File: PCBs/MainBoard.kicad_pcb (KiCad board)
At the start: 2 copper layers, 40.4 x 70 mm, 75 parts, among them J1 USB_C_Receptacle, J2 Conn_01x12_FPC_0.5mm, J3 Conn_01x08, J4 Qwiic_RA, SW1 PTH_RA_h7.5mm, SW2 SMD_4.6x2.8mm_h2.5mm, SW3 SMD_4.6x2.8mm_h2.5mm, U1 TVS_ESD_USB, U2 ESP32-S3-MINI, U3 AP3012, U4 MQ-4 Gas Sensor, U5 PASCO2V01BUMA1, U6 AP2112K-3.3, U7 MQ-7 Gas Sensor, U8 SEN55

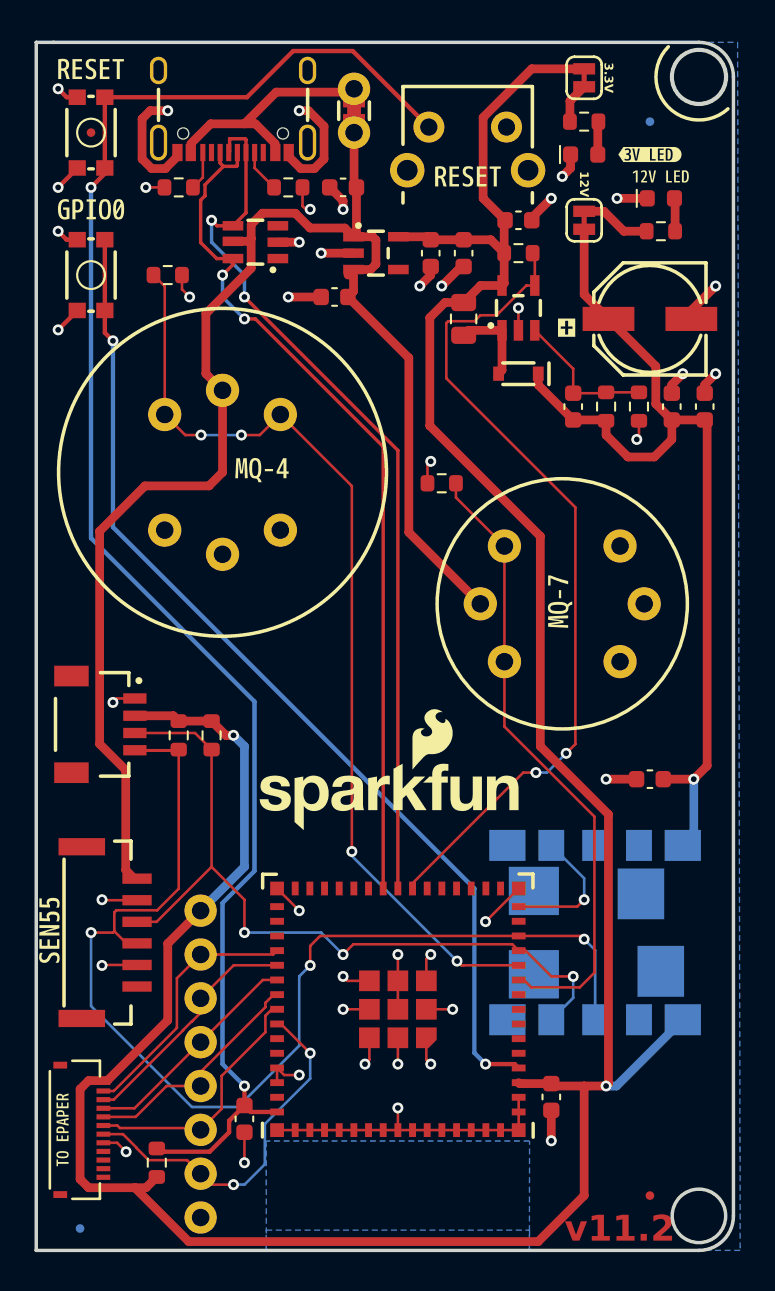
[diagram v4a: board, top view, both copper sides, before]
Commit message: Current PCB updates
Updated Main Board MQ sensors and external reset button position as well as SEN 55 connector pinout.
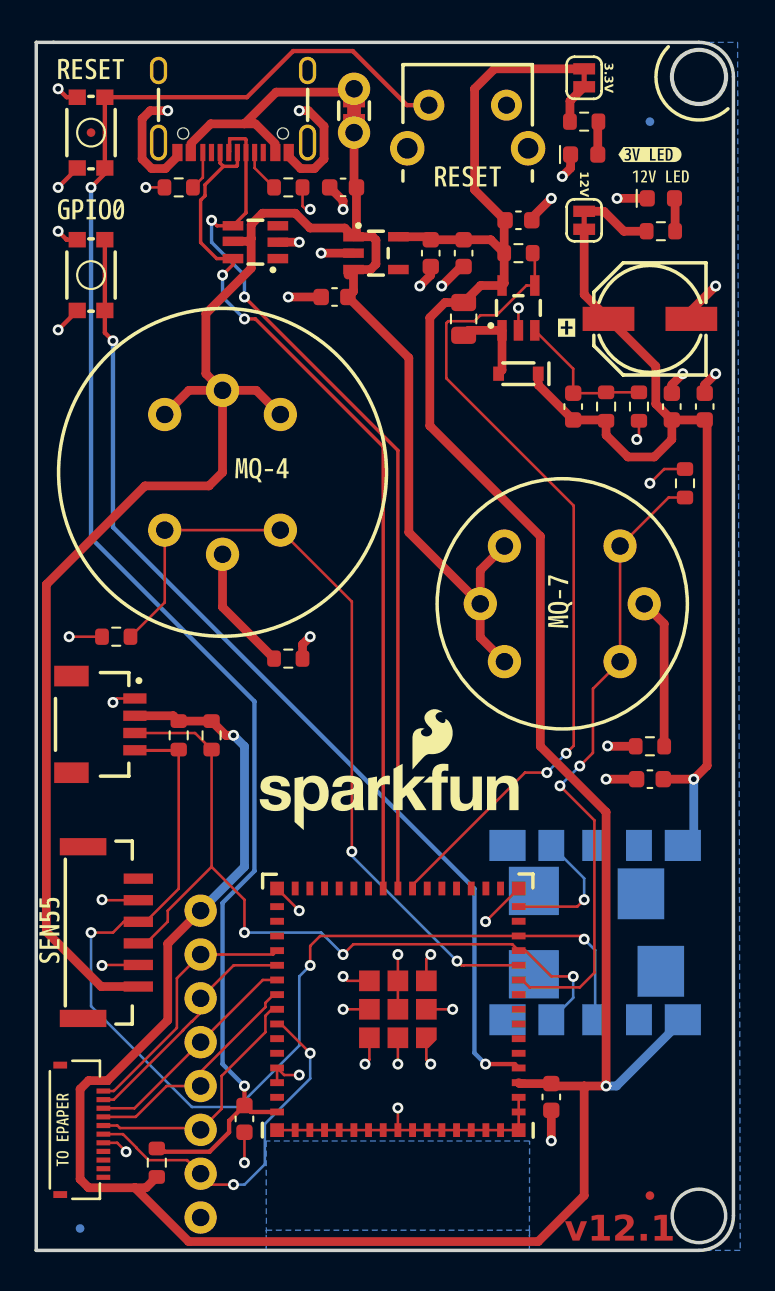
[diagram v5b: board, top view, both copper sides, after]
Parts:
- removed kibuzzard-65B1E438: G***, kibuzzard-65B1E438
- added R13: 100, SparkFun-Resistor:R_0603_1608Metric, F.Cu at (143.4, 89.6)
- added R14: 100, SparkFun-Resistor:R_0603_1608Metric, F.Cu at (164.4, 94.7)
- added kibuzzard-65E78438: G***, kibuzzard-65E78438, B.Cu at (148.9, 82.5)
- moved R7 21.2 mm to (133.4, 88.3), turned to 180 degrees
- moved R11 14.1 mm to (166.4, 79.5), turned to 90 degrees
- moved SW1 1.27 mm to (153.8, 57.5)
- moved U8 0.07 mm to (131.4, 105.5)
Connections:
- C7 pad +: (no net) -> +12V
- C7 pad -: (no net) -> GND
- U4 pad 1: ESP11/MQ4 -> +5V
- U4 pad 3: ESP11/MQ4 -> +5V
- U4 pad 4: GND -> ESP11/MQ4
- U4 pad 5: GND -> Net-(U4-H-)
- U4 pad 6: GND -> ESP11/MQ4
- U7 pad 1: ESP10/MQ7 -> +5V
- U7 pad 3: ESP10/MQ7 -> +5V
- U7 pad 4: GND -> ESP10/MQ7
- U7 pad 5: GND -> Net-(U7-H-)
- U7 pad 6: GND -> ESP10/MQ7
- U8 pad 1: +5V -> unconnected-(U8-NC-Pad1)
- U8 pad 3: SDA -> SCL
- U8 pad 4: SCL -> SDA
- U8 pad 6: unconnected-(U8-NC-Pad6) -> +5V
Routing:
- net +5V: track 86.9 -> 112.6 mm
- net ESP11/MQ4: track 55.7 -> 46.6 mm, vias 4 -> 2
- net Net-(U7-H-): track 0.00 -> 8.73 mm
- net Net-(U4-H-): track 0.00 -> 7.28 mm
- net GND: track 97.6 -> 102.1 mm, vias 43 -> 45
- net SCL: track 68.9 -> 66.8 mm
- net +3.3V: track 165.8 -> 167.3 mm
- net SDA: track 45.8 -> 46.3 mm
- net RESET: track 94.4 -> 93.9 mm
- net ESP10/MQ7: track 36.6 -> 36.8 mm, vias 0 -> 2
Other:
- board text added: "v12.1"
- board text removed: "v11.2"

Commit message: Screen and Main Board Updates
Updated Main board to Screen PCB connection, added accelerometer to Epaper display PCB. Removed GPIO 0 PB and replaced external Reset button with GPIO0 button.
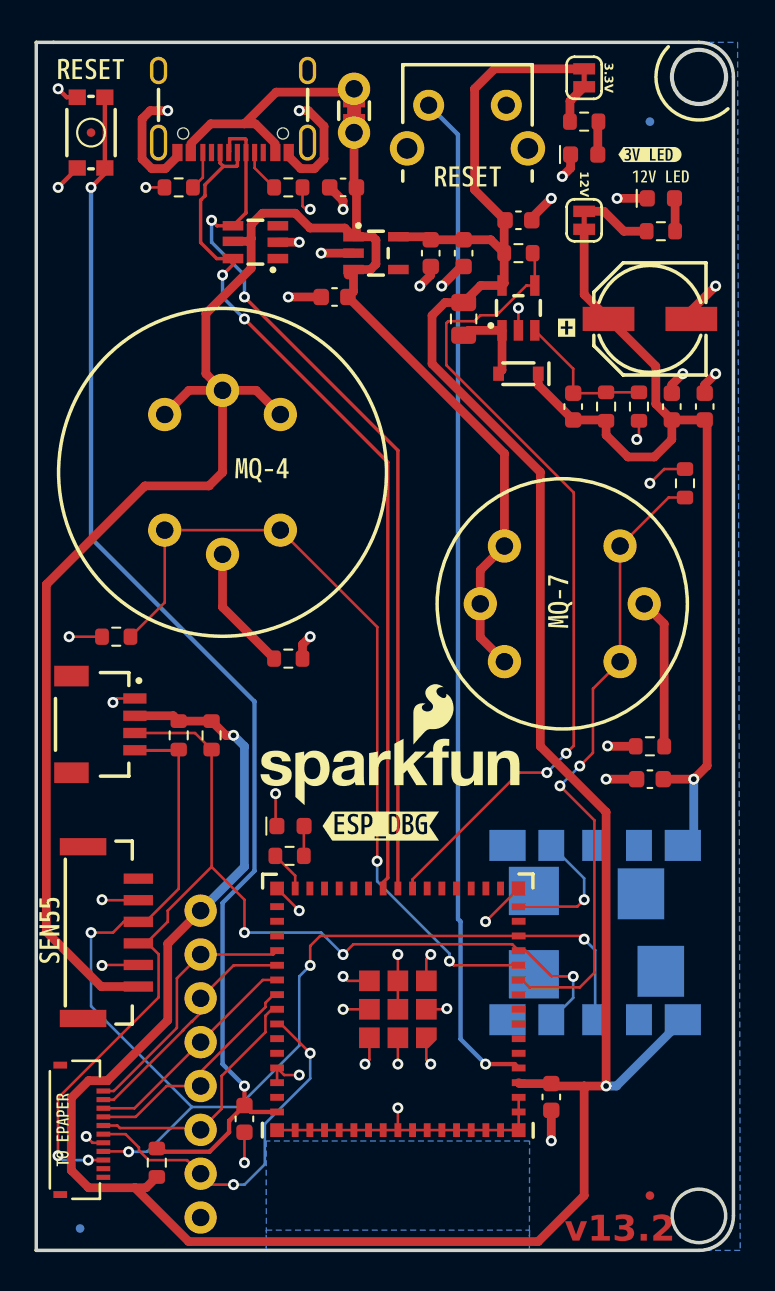
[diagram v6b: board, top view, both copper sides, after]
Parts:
- removed SW3: SMD_4.6x2.8mm_h2.5mm, SparkFun-Switch:Momentary_SMD_4.6x2.8mm_h2.5mm
- removed kibuzzard-65B1D57E: G***, kibuzzard-65B1D57E
- removed kibuzzard-65E78438: G***, kibuzzard-65E78438
- added D4: Red, SparkFun-LED:LED_0603_1608Metric, F.Cu at (143.5, 99.3)
- added R15: 220_0603, SparkFun-Resistor:R_0603_1608Metric, F.Cu at (143.5, 101.0)
- added kibuzzard-65ECB56E: G***, kibuzzard-65ECB56E, F.Cu at (148.8, 99.3)
- added kibuzzard-65ECB59C: G***, kibuzzard-65ECB59C, B.Cu at (148.9, 82.5)
- moved G*** 1.45 mm to (149.1, 96.0)
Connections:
- J2 pad 10: unconnected-(J2-Pin_10-Pad10) -> SDA
- J2 pad 9: unconnected-(J2-Pin_9-Pad9) -> SCL
- SW1 pad 2: RESET -> ESP0
- U2 pad 30: unconnected-(U2-IO48-Pad30) -> ESP DBG
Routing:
- net RESET: track 93.9 -> 72.7 mm
- net SDA: track 46.3 -> 64.6 mm, vias 3 -> 5
- net SCL: track 66.8 -> 73.0 mm, vias 3 -> 4
- net +5V: track 112.6 -> 109.9 mm
- net ESP DBG: track 0.00 -> 2.37 mm
- net Net-(D4-A): track 0.00 -> 1.73 mm
- net GND: track 102.1 -> 100.4 mm, vias 45 -> 44
- net ESP0: vias 2 -> 1
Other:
- board text added: "v13.2"
- board text removed: "v12.1"

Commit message: Updated Main Board PCB
Removed H- resistors to GND from schematic and PCB after confirmed testing that we don't need them.
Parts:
- removed R13, R14: 100, SparkFun-Resistor:R_0603_1608Metric
- removed kibuzzard-65ECB59C: G***, kibuzzard-65ECB59C
- added kibuzzard-65F133B7: G***, kibuzzard-65F133B7, B.Cu at (148.9, 82.5)
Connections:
- C7 pad +: +12V -> (no net)
- C7 pad -: GND -> (no net)
- U4 pad 5: Net-(U4-H-) -> GND
- U7 pad 5: Net-(U7-H-) -> GND
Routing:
- net Net-(U7-H-): track 8.73 -> 0.00 mm
- net Net-(U4-H-): track 7.28 -> 0.00 mm
- net GND: track 100.4 -> 97.3 mm, vias 44 -> 42
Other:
- board text added: "v13.3"
- board text removed: "v13.2"

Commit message: Update Main Board V13.4
Replaced resistor on MQ sensor for resistor that is said to use on data sheet. from 4.7k ohm to 10k ohm.
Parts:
- removed kibuzzard-65F133B7: G***, kibuzzard-65F133B7
- added kibuzzard-65F1350E: G***, kibuzzard-65F1350E, B.Cu at (148.9, 82.5)
- R11, R7: value 4.7k -> 10k
- moved R7 0.19 mm to (133.2, 88.3)
- moved R11 0.13 mm to (166.3, 79.5)
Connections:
- C7 pad +: (no net) -> +12V
- C7 pad -: (no net) -> GND
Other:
- board text added: "v13.4"
- board text removed: "v13.3"
